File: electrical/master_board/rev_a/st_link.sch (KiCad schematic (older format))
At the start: 1 part, among them CN58 STADAPTER;F2x4

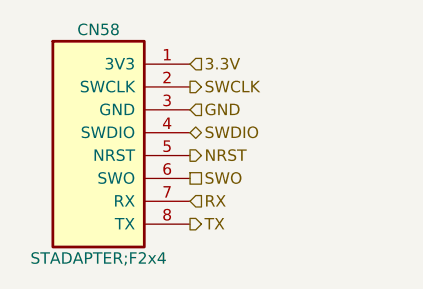
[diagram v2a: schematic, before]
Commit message: Bound signals to Morpho pins.
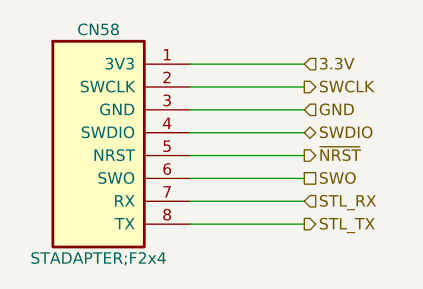
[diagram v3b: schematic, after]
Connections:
- net NRST renamed ~NRST
- net RX renamed STL_RX
- net TX renamed STL_TX
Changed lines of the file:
@@
 $Descr A4 11693 8268
 encoding utf-8
-Sheet 7 10
+Sheet 4 10
 Title "HR2 ST-Link"
 Date "2020-10-17"
@@
 Comment4 ""
 $EndDescr
-Text HLabel 6000 3650 2    50   Input ~ 0
+Text HLabel 6500 3650 2    50   Input ~ 0
 3.3V
-Text HLabel 6000 3750 2    50   Output ~ 0
+Text HLabel 6500 3750 2    50   Output ~ 0
 SWCLK
-Text HLabel 6000 3850 2    50   Input ~ 0
+Text HLabel 6500 3850 2    50   Input ~ 0
 GND
-Text HLabel 6000 3950 2    50   BiDi ~ 0
+Text HLabel 6500 3950 2    50   BiDi ~ 0
 SWDIO
-Text HLabel 6000 4050 2    50   Output ~ 0
-NRST
-Text HLabel 6000 4150 2    50   UnSpc ~ 0
+Text HLabel 6500 4050 2    50   Output ~ 0
+~NRST
+Text HLabel 6500 4150 2    50   UnSpc ~ 0
 SWO
-Text HLabel 6000 4250 2    50   Input ~ 0
-RX
-Text HLabel 6000 4350 2    50   Output ~ 0
-TX
+Text HLabel 6500 4250 2    50   Input ~ 0
+STL_RX
+Text HLabel 6500 4350 2    50   Output ~ 0
+STL_TX
 $Comp
 L HR2:STADAPTER;F2x4 CN58
@@
 	1    0    0    -1
 $EndComp
+Wire Wire Line
+	6000 3650 6500 3650
+Wire Wire Line
+	6500 3750 6000 3750
+Wire Wire Line
+	6000 3850 6500 3850
+Wire Wire Line
+	6500 3950 6000 3950
+Wire Wire Line
+	6000 4050 6500 4050
+Wire Wire Line
+	6500 4150 6000 4150
+Wire Wire Line
+	6000 4250 6500 4250
+Wire Wire Line
+	6000 4350 6500 4350
 $EndSCHEMATC

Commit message: Reannoted. Postioned components are in the 80-99 reference range.
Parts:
- renumbered CN58 to CN90
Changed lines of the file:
@@
 STL_TX
 $Comp
-L HR2:STADAPTER;F2x4 CN58
+L HR2:STADAPTER;F2x4 CN90
 U 1 1 5F4B5155
 P 5200 3650
-F 0 "CN58" H 5600 3800 50  0000 C CNN
+F 0 "CN90" H 5600 3800 50  0000 C CNN
 F 1 "STADAPTER;F2x4" H 5600 2800 50  0000 C CNN
 F 2 "HR2:STADAPTER_F2x4" H 5400 3700 60  0001 L CNN
